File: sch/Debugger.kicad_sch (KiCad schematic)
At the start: 25 parts, among them J3 Conn_ARM_SWD_TagConnect_TC203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, Q1 Q_NMOS_GSD, U10 TPS22991, U6 TXU0204RUTR, U7 nRF52833-QDXX, U8 TXU0101DRYR, Y2 32MHz, 10pF

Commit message: Updates for rev 1
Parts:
- added D5: LED_Blue, LED_SMD:LED_0603_1608Metric, symbol Device:LED_Small
- added R17: 1kR, passives:C_0201_0603Metric_L, symbol Device:R_Small_US
- added TP32, TP33, TP34, TP35: TestPoint, TestPoint:TestPoint_Pad_D1.0mm, symbol Connector:TestPoint
- C35, C40: LCSC (none) -> C335103
- C36, C41, C42, C43, C46, C47, C48, C49, C50, C51: LCSC (none) -> C76935
- C37: LCSC (none) -> C62550
- C38: LCSC (none) -> C467016
- C39: LCSC (none) -> C23733
- C44, C45: LCSC (none) -> C384960
- Q1: LCSC (none) -> C19949844
- R8: LCSC (none) -> C106224
- U10: LCSC (none) -> C49307573
- U6: LCSC (none) -> C5217875
- U7: LCSC (none) -> C3007767
- U8: LCSC (none) -> C5217869
- Y2: LCSC (none) -> C383840
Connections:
- net DBG_SWDIO_OE: now also TP34.1
- net DBG_VDD: now also TP32.1
- net DBG_~{RESET}: now also TP35.1
- net GND: now also R17.2
- net LEVEL_SHIFT_VDD: now also TP33.1
- net at U7.22 (P0.09): now also D5.2 (A)
- new net: D5.1 (K), R17.1
- no-connect marks 13 -> 12

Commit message: Updates
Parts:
- D5: LCSC C965807 -> C7496819
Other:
- moved on the sheet: C50, C51

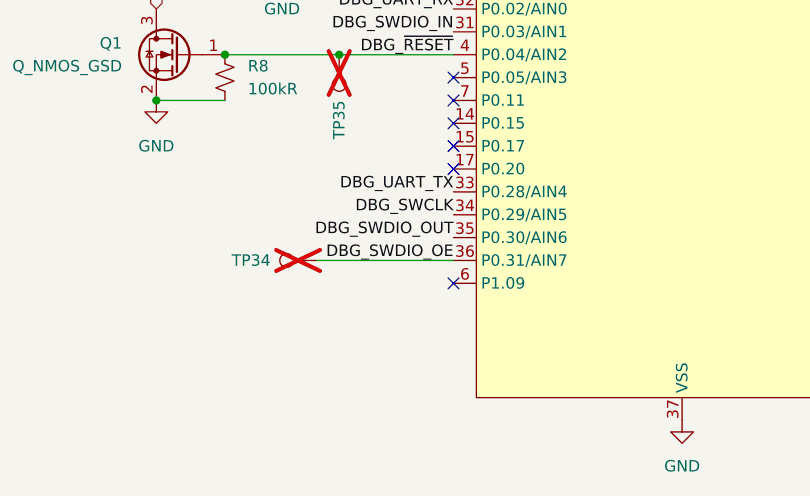
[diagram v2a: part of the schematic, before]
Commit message: Added external current measurement for L15 and SX1262
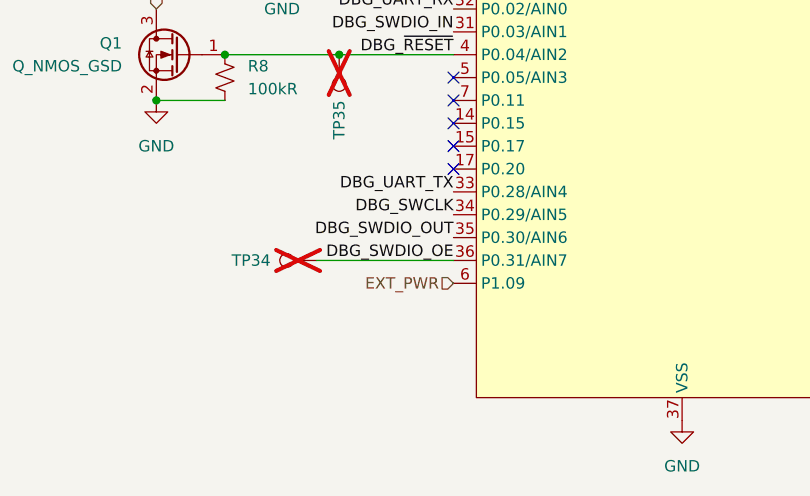
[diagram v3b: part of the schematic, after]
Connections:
- net EXT_PWR: now reaches U7.6 (P1.09)
- no-connect marks 12 -> 11
